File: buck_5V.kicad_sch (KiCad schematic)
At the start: 15 parts, among them U1501 TPS566238RQFR

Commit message: Reannotate components
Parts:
- renumbered C1502 to C1001, C1503 to C1002, C1510 to C1003, C1501 to C1004, C1509 to C1005, C1505 to C1006, C1504 to C1007, C1506 to C1008, L1501 to L1001, R1502 to R1001, R1501 to R1002, R1503 to R1003, TP1501 to TP1001, TP1502 to TP1002, U1501 to U1001
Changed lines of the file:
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@@
 		(on_board yes)
 		(dnp no)
-		(property "Reference" "#PWR01504"
+		(property "Reference" "#PWR01007"
 			(at 191.77 96.52 0)
 			(effects
@@
 			(project "SH-RPi"
 				(path "/abc482bd-3f17-4d35-80db-1da3dcdb5c27/c7bf4e1f-6bd1-4be7-9e56-1bd438bf5d42/531e3be9-7113-42c4-b43f-4c940587f1bb"
-					(reference "#PWR01504")
+					(reference "#PWR01007")
 					(unit 1)
 				)
@@
 		(on_board yes)
 		(dnp no)
-		(property "Reference" "#PWR01508"
+		(property "Reference" "#PWR01008"
 			(at 204.47 101.6 0)
 			(effects
@@
 			(project "SH-RPi"
 				(path "/abc482bd-3f17-4d35-80db-1da3dcdb5c27/c7bf4e1f-6bd1-4be7-9e56-1bd438bf5d42/531e3be9-7113-42c4-b43f-4c940587f1bb"
-					(reference "#PWR01508")
+					(reference "#PWR01008")
 					(unit 1)
 				)
@@
 		(on_board yes)
 		(dnp no)
-		(property "Reference" "C1509"
+		(property "Reference" "C1005"
 			(at 159.639 83.9216 0)
 			(effects
@@
 			(project "Yellow"
 				(path "/abc482bd-3f17-4d35-80db-1da3dcdb5c27/c7bf4e1f-6bd1-4be7-9e56-1bd438bf5d42/531e3be9-7113-42c4-b43f-4c940587f1bb"
-					(reference "C1509")
+					(reference "C1005")
 					(unit 1)
 				)
@@
 		(on_board yes)
 		(dnp no)
-		(property "Reference" "#PWR01510"
+		(property "Reference" "#PWR01004"
 			(at 102.87 109.22 0)
 			(effects
@@
 			(project "Yellow"
 				(path "/abc482bd-3f17-4d35-80db-1da3dcdb5c27/c7bf4e1f-6bd1-4be7-9e56-1bd438bf5d42/531e3be9-7113-42c4-b43f-4c940587f1bb"
-					(reference "#PWR01510")
+					(reference "#PWR01004")
 					(unit 1)
 				)
@@
 		(on_board yes)
 		(dnp no)
-		(property "Reference" "R1502"
+		(property "Reference" "R1001"
 			(at 76.2 90.424 90)
 			(effects
@@
 			(project ""
 				(path "/abc482bd-3f17-4d35-80db-1da3dcdb5c27/c7bf4e1f-6bd1-4be7-9e56-1bd438bf5d42/531e3be9-7113-42c4-b43f-4c940587f1bb"
-					(reference "R1502")
+					(reference "R1001")
 					(unit 1)
 				)
@@
 		(dnp no)
 		(fields_autoplaced yes)
-		(property "Reference" "#FLG01501"
+		(property "Reference" "#FLG01001"
 			(at 195.58 70.485 0)
 			(effects
@@
 			(project "SH-RPi"
 				(path "/abc482bd-3f17-4d35-80db-1da3dcdb5c27/c7bf4e1f-6bd1-4be7-9e56-1bd438bf5d42/531e3be9-7113-42c4-b43f-4c940587f1bb"
-					(reference "#FLG01501")
+					(reference "#FLG01001")
 					(unit 1)
 				)
@@
 		(on_board yes)
 		(dnp no)
-		(property "Reference" "TP1502"
+		(property "Reference" "TP1002"
 			(at 224.79 85.8519 0)
 			(effects
@@
 			(project "Yellow"
 				(path "/abc482bd-3f17-4d35-80db-1da3dcdb5c27/c7bf4e1f-6bd1-4be7-9e56-1bd438bf5d42/531e3be9-7113-42c4-b43f-4c940587f1bb"
-					(reference "TP1502")
+					(reference "TP1002")
 					(unit 1)
 				)
@@
 		(dnp no)
 		(fields_autoplaced yes)
-		(property "Reference" "U1501"
+		(property "Reference" "U1001"
 			(at 102.87 59.69 0)
 			(effects
@@
 			(project ""
 				(path "/abc482bd-3f17-4d35-80db-1da3dcdb5c27/c7bf4e1f-6bd1-4be7-9e56-1bd438bf5d42/531e3be9-7113-42c4-b43f-4c940587f1bb"
-					(reference "U1501")
+					(reference "U1001")
 					(unit 1)
 				)
@@
 		(on_board yes)
 		(dnp no)
-		(property "Reference" "R1503"
+		(property "Reference" "R1003"
 			(at 206.248 89.0016 0)
 			(effects
@@
 			(project "SH-RPi"
 				(path "/abc482bd-3f17-4d35-80db-1da3dcdb5c27/c7bf4e1f-6bd1-4be7-9e56-1bd438bf5d42/531e3be9-7113-42c4-b43f-4c940587f1bb"
-					(reference "R1503")
+					(reference "R1003")
 					(unit 1)
 				)
@@
 		(on_board yes)
 		(dnp no)
-		(property "Reference" "#PWR01502"
+		(property "Reference" "#PWR01002"
 			(at 50.8 93.98 0)
 			(effects
@@
 			(project "Yellow"
 				(path "/abc482bd-3f17-4d35-80db-1da3dcdb5c27/c7bf4e1f-6bd1-4be7-9e56-1bd438bf5d42/531e3be9-7113-42c4-b43f-4c940587f1bb"
-					(reference "#PWR01502")
+					(reference "#PWR01002")
 					(unit 1)
 				)
@@
 		(on_board yes)
 		(dnp no)
-		(property "Reference" "L1501"
+		(property "Reference" "L1001"
 			(at 154.94 67.564 90)
 			(effects
@@
 			(project "Yellow"
 				(path "/abc482bd-3f17-4d35-80db-1da3dcdb5c27/c7bf4e1f-6bd1-4be7-9e56-1bd438bf5d42/531e3be9-7113-42c4-b43f-4c940587f1bb"
-					(reference "L1501")
+					(reference "L1001")
 					(unit 1)
 				)
@@
 		(on_board yes)
 		(dnp no)
-		(property "Reference" "R1501"
+		(property "Reference" "R1002"
 			(at 208.28 77.47 0)
 			(effects
@@
 			(project "SH-RPi"
 				(path "/abc482bd-3f17-4d35-80db-1da3dcdb5c27/c7bf4e1f-6bd1-4be7-9e56-1bd438bf5d42/531e3be9-7113-42c4-b43f-4c940587f1bb"
-					(reference "R1501")
+					(reference "R1002")
 					(unit 1)
 				)
@@
 		(on_board yes)
 		(dnp no)
-		(property "Reference" "#PWR01501"
+		(property "Reference" "#PWR01001"
 			(at 36.83 93.98 0)
 			(effects
@@
 			(project "SH-RPi"
 				(path "/abc482bd-3f17-4d35-80db-1da3dcdb5c27/c7bf4e1f-6bd1-4be7-9e56-1bd438bf5d42/531e3be9-7113-42c4-b43f-4c940587f1bb"
-					(reference "#PWR01501")
+					(reference "#PWR01001")
 					(unit 1)
 				)
@@
 		(on_board yes)
 		(dnp no)
-		(property "Reference" "TP1501"
+		(property "Reference" "TP1001"
 			(at 137.16 74.4219 0)
 			(effects
@@
 			(project "SH-RPi"
 				(path "/abc482bd-3f17-4d35-80db-1da3dcdb5c27/c7bf4e1f-6bd1-4be7-9e56-1bd438bf5d42/531e3be9-7113-42c4-b43f-4c940587f1bb"
-					(reference "TP1501")
+					(reference "TP1001")
 					(unit 1)
 				)
@@
 		(on_board yes)
 		(dnp no)
-		(property "Reference" "C1506"
+		(property "Reference" "C1008"
 			(at 218.821 77.5716 0)
 			(effects
@@
 			(project "Yellow"
 				(path "/abc482bd-3f17-4d35-80db-1da3dcdb5c27/c7bf4e1f-6bd1-4be7-9e56-1bd438bf5d42/531e3be9-7113-42c4-b43f-4c940587f1bb"
-					(reference "C1506")
+					(reference "C1008")
 					(unit 1)
 				)
@@
 		(on_board yes)
 		(dnp no)
-		(property "Reference" "C1501"
+		(property "Reference" "C1004"
 			(at 146.05 60.96 90)
 			(effects
@@
 			(project "SH-RPi"
 				(path "/abc482bd-3f17-4d35-80db-1da3dcdb5c27/c7bf4e1f-6bd1-4be7-9e56-1bd438bf5d42/531e3be9-7113-42c4-b43f-4c940587f1bb"
-					(reference "C1501")
+					(reference "C1004")
 					(unit 1)
 				)
@@
 		(on_board yes)
 		(dnp no)
-		(property "Reference" "C1504"
+		(property "Reference" "C1007"
 			(at 188.849 77.5716 0)
 			(effects
@@
 			(project "HALPI2"
 				(path "/abc482bd-3f17-4d35-80db-1da3dcdb5c27/c7bf4e1f-6bd1-4be7-9e56-1bd438bf5d42/531e3be9-7113-42c4-b43f-4c940587f1bb"
-					(reference "C1504")
+					(reference "C1007")
 					(unit 1)
 				)
@@
 		(on_board yes)
 		(dnp no)
-		(property "Reference" "C1510"
+		(property "Reference" "C1003"
 			(at 64.389 95.3516 0)
 			(effects
@@
 			(project "Yellow"
 				(path "/abc482bd-3f17-4d35-80db-1da3dcdb5c27/c7bf4e1f-6bd1-4be7-9e56-1bd438bf5d42/531e3be9-7113-42c4-b43f-4c940587f1bb"
-					(reference "C1510")
+					(reference "C1003")
 					(unit 1)
 				)
@@
 		(on_board yes)
 		(dnp no)
-		(property "Reference" "C1503"
+		(property "Reference" "C1002"
 			(at 47.879 75.0316 0)
 			(effects
@@
 			(project "Yellow"
 				(path "/abc482bd-3f17-4d35-80db-1da3dcdb5c27/c7bf4e1f-6bd1-4be7-9e56-1bd438bf5d42/531e3be9-7113-42c4-b43f-4c940587f1bb"
-					(reference "C1503")
+					(reference "C1002")
 					(unit 1)
 				)
@@
 		(on_board yes)
 		(dnp no)
-		(property "Reference" "#PWR01505"
+		(property "Reference" "#PWR01006"
 			(at 172.72 96.52 0)
 			(effects
@@
 			(project "HALPI2"
 				(path "/abc482bd-3f17-4d35-80db-1da3dcdb5c27/c7bf4e1f-6bd1-4be7-9e56-1bd438bf5d42/531e3be9-7113-42c4-b43f-4c940587f1bb"
-					(reference "#PWR01505")
+					(reference "#PWR01006")
 					(unit 1)
 				)
@@
 		(on_board yes)
 		(dnp no)
-		(property "Reference" "C1502"
+		(property "Reference" "C1001"
 			(at 33.909 75.0316 0)
 			(effects
@@
 			(project "SH-RPi"
 				(path "/abc482bd-3f17-4d35-80db-1da3dcdb5c27/c7bf4e1f-6bd1-4be7-9e56-1bd438bf5d42/531e3be9-7113-42c4-b43f-4c940587f1bb"
-					(reference "C1502")
+					(reference "C1001")
 					(unit 1)
 				)
@@
 		(on_board yes)
 		(dnp no)
-		(property "Reference" "#PWR01503"
+		(property "Reference" "#PWR01005"
 			(at 162.56 96.52 0)
 			(effects
@@
 			(project "Yellow"
 				(path "/abc482bd-3f17-4d35-80db-1da3dcdb5c27/c7bf4e1f-6bd1-4be7-9e56-1bd438bf5d42/531e3be9-7113-42c4-b43f-4c940587f1bb"
-					(reference "#PWR01503")
+					(reference "#PWR01005")
 					(unit 1)
 				)
@@
 		(on_board yes)
 		(dnp no)
-		(property "Reference" "#PWR01509"
+		(property "Reference" "#PWR01003"
 			(at 67.31 109.22 0)
 			(effects
@@
 			(project "Yellow"
 				(path "/abc482bd-3f17-4d35-80db-1da3dcdb5c27/c7bf4e1f-6bd1-4be7-9e56-1bd438bf5d42/531e3be9-7113-42c4-b43f-4c940587f1bb"
-					(reference "#PWR01509")
+					(reference "#PWR01003")
 					(unit 1)
 				)
@@
 		(on_board yes)
 		(dnp no)
-		(property "Reference" "C1505"
+		(property "Reference" "C1006"
 			(at 169.799 80.1116 0)
 			(effects
@@
 			(project "HALPI2"
 				(path "/abc482bd-3f17-4d35-80db-1da3dcdb5c27/c7bf4e1f-6bd1-4be7-9e56-1bd438bf5d42/531e3be9-7113-42c4-b43f-4c940587f1bb"
-					(reference "C1505")
-					(unit 1)
-				)
+					(reference "C1006")
+					(unit 1)
+				)

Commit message: Most DRC errors fixed
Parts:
- C1001: value 47uF -> 10uF; footprint Capacitor_SMD:C_1210_3225Metric -> Capacitor_SMD:C_1206_3216Metric; LCSC C5440143 -> C13585
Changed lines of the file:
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@@
 			)
 		)
-		(property "Value" "47uF"
+		(property "Value" "10uF"
 			(at 33.909 77.343 0)
 			(effects
@@
 			)
 		)
-		(property "Footprint" "Capacitor_SMD:C_1210_3225Metric"
+		(property "Footprint" "Capacitor_SMD:C_1206_3216Metric"
 			(at 35.8648 80.01 0)
 			(effects
@@
 			)
 		)
-		(property "LCSC" "C5440143"
+		(property "LCSC" "C13585"
 			(at 36.83 76.2 0)
 			(effects

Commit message: Silkscreen mostly done
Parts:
- added J1001: 5V Header, Connector_PinHeader_2.54mm:PinHeader_2x02_P2.54mm_Vertical, symbol Connector_Generic:Conn_02x02_Odd_Even
- C1002, C1005: value 100nF -> 1uF; LCSC C1525 -> C52923
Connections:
- net GND: now also J1001.1 (Pin_1), J1001.3 (Pin_3)
- net Vout: now also J1001.2 (Pin_2), J1001.4 (Pin_4)

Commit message: Further refinements
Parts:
- R1002: value 100k -> 220k; LCSC C25803 -> C22961
- R1003: value 22k -> 30k; LCSC C31850 -> C22984
- U1001: value TPS566238RQFR -> TPS566238PRQFR; LCSC C5219353 -> C2876603

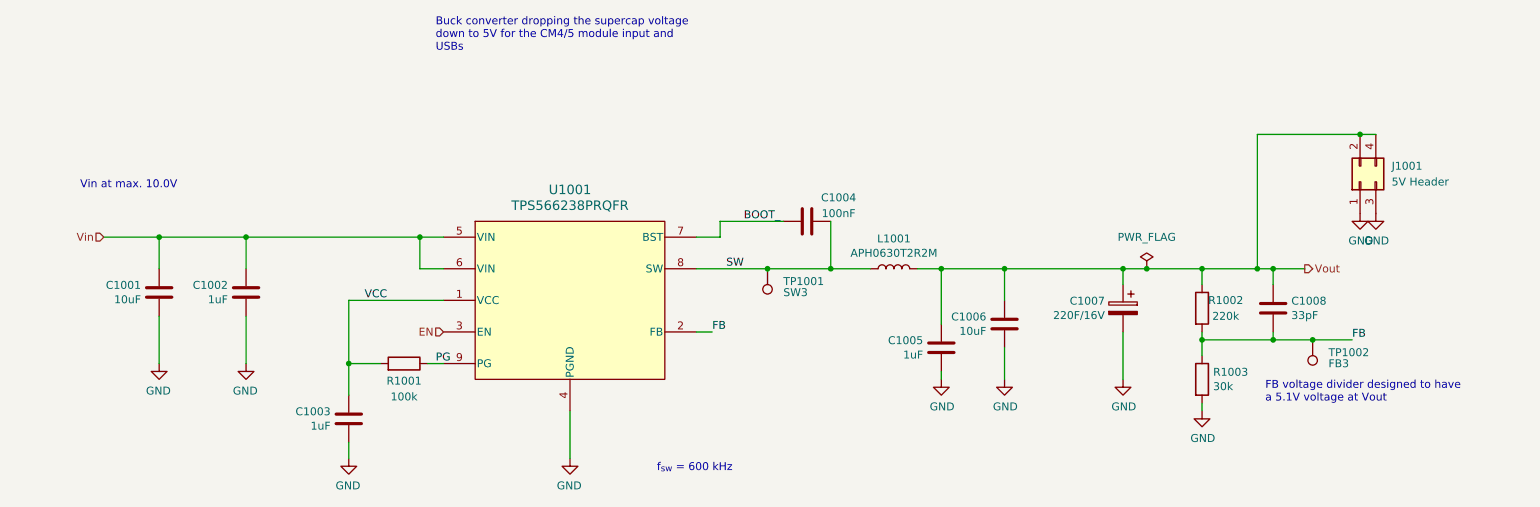
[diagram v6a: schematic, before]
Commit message: Finish transitioning to RP2040
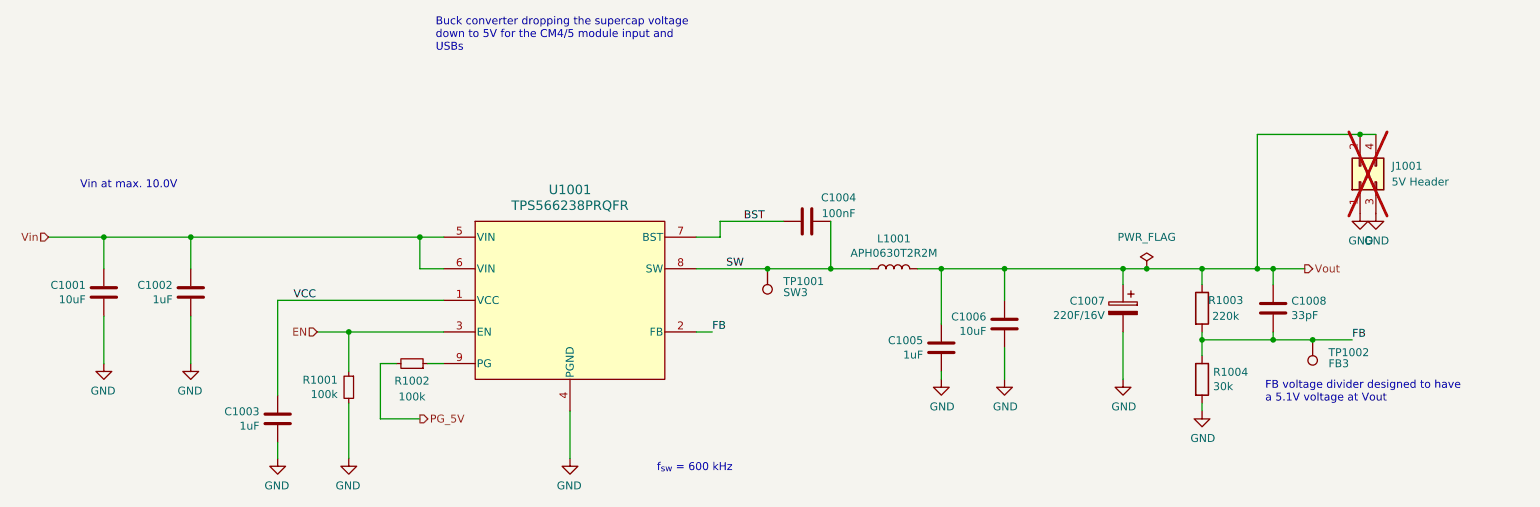
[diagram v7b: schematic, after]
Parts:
- added R1001: 100k, Resistor_SMD:R_0402_1005Metric, symbol Device:R_Small
- J1001: LCSC (none) -> C7501273; now not fitted; now in the parts list
- R1002: renamed from R1001; symbol Device:R -> Device:R_Small
- renumbered R1002 to R1003, R1003 to R1004
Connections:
- net EN: now also R1001.1
- net GND: now also R1001.2
- net VCC: no longer R1002.2
- net BOOT_ renamed BST
- net PG: no longer names the net of R1002.1, U1001.9 (PG)
- new net PG_5V: R1002.2
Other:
- moved on the sheet: C1001, C1002, C1003, R1002

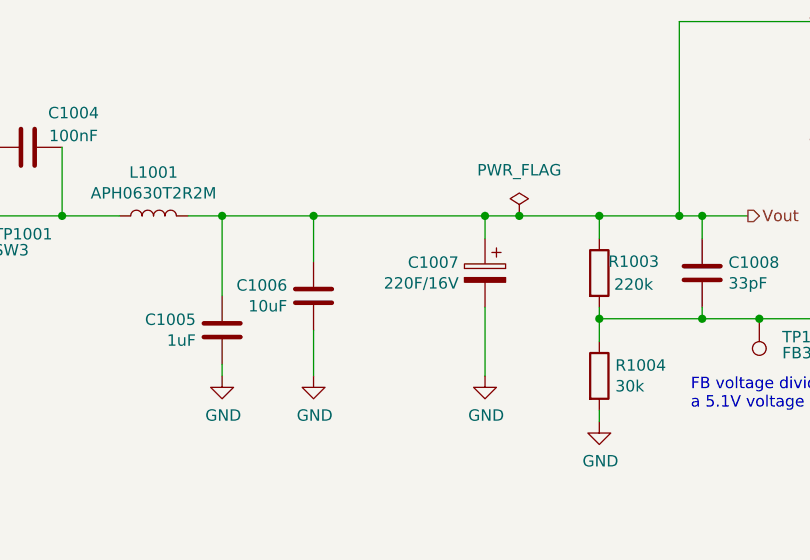
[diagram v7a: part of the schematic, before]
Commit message: Apply part PCBA position corrections
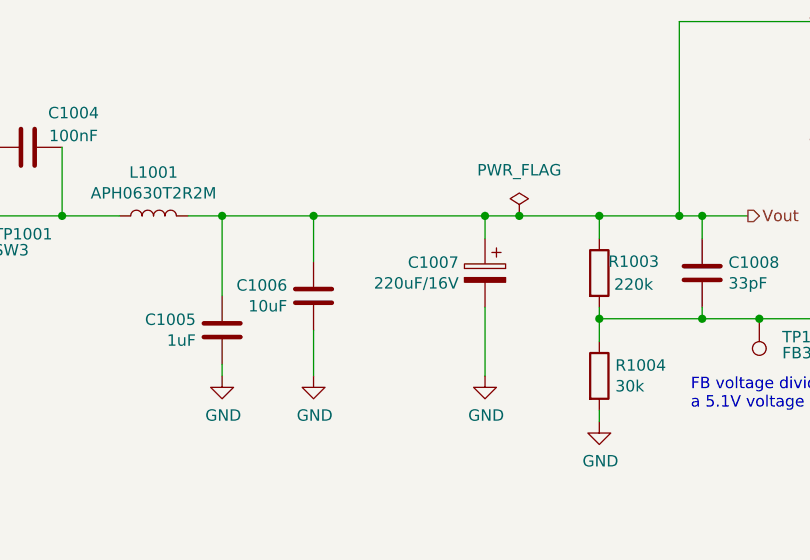
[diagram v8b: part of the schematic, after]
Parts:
- C1007: value 220F/16V -> 220uF/16V
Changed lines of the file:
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@@
 			)
 		)
-		(property "Value" "220F/16V"
+		(property "Value" "220uF/16V"
 			(at 188.849 79.883 0)
 			(effects
